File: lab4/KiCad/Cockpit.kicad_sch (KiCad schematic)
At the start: 24 parts, among them J30 CAN A isolation, J31 CAN A test, J34 CAN B isolation, J35 CAN B test, U30 MCP2515T-I/ST, U31 SN65HVD231MDREP, U34 MCP2515T-I/ST, U35 SN65HVD231MDREP, Y30 16 MHz, Y34 16 MHz

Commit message: Integrate Lab 4 MCU support, diagnostics and hierarchical connections
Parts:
- added C700: 22u /16V, Capacitor_SMD:C_0805_2012Metric, symbol Device:C
- added C701: 100n, Capacitor_SMD:C_0603_1608Metric, symbol Device:C
- added C702: 100n TEST, Capacitor_SMD:C_0603_1608Metric, symbol Device:C
- added D710: STATUS green, LED_SMD:LED_0603_1608Metric, symbol Device:LED
- added D711: ERR red, LED_SMD:LED_0603_1608Metric, symbol Device:LED
- added D712: DEG_A yellow, LED_SMD:LED_0603_1608Metric, symbol Device:LED
- added D713: DEG_B yellow, LED_SMD:LED_0603_1608Metric, symbol Device:LED
- added J70: Raspberry Pi4 GPIO, Connector_PinSocket_2.54mm:PinSocket_2x20_P2.54mm_Vertical, symbol Lab4_Logic:Pi4_Powered_Header
- added J703: LAB3 rows 1-13, Connector_PinHeader_2.54mm:PinHeader_1x13_P2.54mm_Vertical, symbol Connector_Generic:Conn_01x13
- added J704: Pi extra probes, Connector_PinHeader_2.54mm:PinHeader_1x05_P2.54mm_Vertical, symbol Connector_Generic:Conn_01x05
- added R700: 10k TEST pullup, Resistor_SMD:R_0603_1608Metric, symbol Device:R
- added R710, R711, R712, R713: 1k, Resistor_SMD:R_0603_1608Metric, symbol Device:R
- added SW70: SWT0210-045026GSA, symbol Switch:SW_Push
- U30, U34: symbol Interface_CAN_LIN:MCP2515-xST -> Lab4_Logic:MCP2515_TSSOP20
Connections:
- net +3V3: now also R700.1
- net GND: now also C700.2, C701.2, C702.2, D710.1 (K), D711.1 (K), D712.1 (K), D713.1 (K), J70.14 (GND), J70.20 (GND), J70.25 (GND), J70.30 (GND), J70.34 (GND), J70.39 (GND), J70.6 (GND), J70.9 (GND), J703.1 (Pin_1), J703.2 (Pin_2), J704.1 (Pin_1), J704.2 (Pin_2), SW70.2
- net PI_CS_A: now also J70.24 (~{CE0}_SPI0/GPIO08)
- net PI_CS_B: now also J70.26 (~{CE1}_SPI0/GPIO07)
- net PI_INT_A: now also J70.22 (GPIO25/SDIO_DAT1)
- net PI_INT_B: now also J70.18 (GPIO24/SDIO_DAT0)
- net PI_MISO: now also J70.21 (MISO_SPI0/GPIO09)
- net PI_MOSI: now also J70.19 (MOSI_SPI0/GPIO10)
- net PI_SCK: now also J70.23 (SCLK_SPI0/GPIO11)
- new net: J70.1 (3V3), J70.17 (3V3)
- new net +5V: C700.1, C701.1, J70.2 (5V), J70.4 (5V)
- new net PI_CMD_TX_MARKER: J70.13 (GPIO27/SDIO_DAT3), J703.4 (Pin_4)
- new net PI_DEG_A_LED: J70.29 (GPCLK1/GPIO05), J703.7 (Pin_7), R712.1
- new net PI_DEG_A_LED_ANODE: D712.2 (A), R712.2
- new net PI_DEG_B_LED: J70.31 (GPCLK2/GPIO06), J703.8 (Pin_8), R713.1
- new net PI_DEG_B_LED_ANODE: D713.2 (A), R713.2
- new net PI_ERROR_LED: J70.32 (GPIO12/PWM0), J704.4 (Pin_4), R711.1
- new net PI_ERROR_LED_ANODE: D711.2 (A), R711.2
- new net PI_SELFTEST_BUTTON: C702.1, J70.36 (GPIO16/SPI1_~{CE2}), J704.3 (Pin_3), R700.2, SW70.1
- new net PI_STATUS_LED: J70.33 (GPIO13/PWM1), J704.5 (Pin_5), R710.1
- new net PI_STATUS_LED_ANODE: D710.2 (A), R710.2
- new net PI_TX_A_MARKER: J70.15 (GPIO22/SDIO_CLK), J703.5 (Pin_5)
- new net PI_TX_B_MARKER: J70.16 (GPIO23/SDIO_CMD), J703.6 (Pin_6)
- new net PI_UDP_RX_MARKER: J70.11 (GPIO17/SPI1_~{CE1}), J703.3 (Pin_3)
- no-connect marks 12 -> 31
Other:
- note added: "All Pi GPIOs are 3.3V signals. Header pin number is NOT BCM GPIO number. Independent board 3.3V supplies the six CAN interfaces. A=CE0/IRQ25; B=CE1/IRQ24; confirm Linux labels against the installed overlay."
- note added: "Local bypass is not a load-step proof. Pi bulk capacitance / rail transient test remains open."
- note added: "Pins 2/4 receive board 5.1V. Pi 3.3V pins 1/17 are NOT joined to board 3.3V. Do not attach independent USB-C power while board 5.1V is connected. Confirm socket orientation with a 1:1 print and the actual Pi before routing."
- note added: "RASPBERRY PI 4 - 40-pin board socket"
- note added: "Rows 9-13 intentionally unused on Pi (Lab3 p17). Two GND pins per probe group. Active-high LED outputs. Physical reachability is a layout check, not established by this schematic."
- note added: "Shared rails and CAN backbone connect through the root sheet. SPI, clocks and reset stay within each zone."
- note removed: "HOST INTERFACE (to be integrated with the bare MCU / Pi header) SPI0: BCM11=SCK, BCM9=MISO, BCM10=MOSI; BCM8=CE0, BCM7=CE1. INT pins: verify against Pi configuration. These named nets are LOCAL to this zone. All +3V3 / +5V / GND / CAN backbone nets need hierarchy ports before full-board integration."
- title: Cockpit zone - dual CAN -> Cockpit zone - integrated logic and interfaces

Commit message: Update Lab 4 circuits, assembly BOMs and measured PCB placement
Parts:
- C300, C301, C340, C341: value Cload TBD -> 18p C0G 50V; Design status (none) -> CL=12pF; equal 18pF caps assume 3pF effective stray; tune a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; MPN (none) -> GRM1885C1H180JA01D
- J70: footprint Connector_PinSocket_2.54mm:PinSocket_2x20_P2.54mm_Vertical -> Lab4_Mechanical:Samtec_ESQ-120-44_2x20_P2.54mm_H18.67; Design status Physical header numbering; select mating height/orientation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 -> Bottom-mounted direct Pi socket; 22mm nominal board gap; ve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; MPN TBD 2x20 female socket -> ESQ-120-44-L-D
- U31, U35: value SN65HVD231MDREP -> SN65HVD231DR; Design status Course Oct 16 substitution; verify exact supplied ordering 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 -> TI verified SOIC-8 order code; confirm course-stock equival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; MPN SN65HVD231MDREP -> SN65HVD231DR

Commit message: Prepare Lab 4 review package and align course assembly plan
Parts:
- C302, C303, C304, C342, C343, C344: Design status (none) -> Preliminary; verify before fabrication; MPN (none) -> KGM15AR71C104KT
- J31, J35, U30, U34: Design status (none) -> Preliminary; verify before fabrication
- R300, R301, R340, R341: Design status (none) -> Preliminary; verify before fabrication; MPN (none) -> CRCW060310K0FKEA
- SW70: Design status Electrical circuit placed; exact GCT footprint drawing stil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 -> GCT drawing located (25-Apr-2025); contact-pair/pad geometr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
- U31, U35: Design status TI verified SOIC-8 order code; confirm course-stock equival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 -> Exact MPN appears in course v3 stock list; TI SOIC-8 pinout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

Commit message: Add verified GCT switch footprints and refresh Lab 4 checks
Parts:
- SW70: footprint (none) -> Lab4_Switches:GCT_SWT0210_4.5x4.5mm; Design status GCT drawing located (25-Apr-2025); contact-pair/pad geometr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 -> GCT A1 drawing verified: physical terminals 1/2 -> logical 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

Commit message: Complete MCU routing and refine feedback and power transitions
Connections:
- net at J70.1 (3V3): no longer J70.17 (3V3)
- no-connect marks 31 -> 32

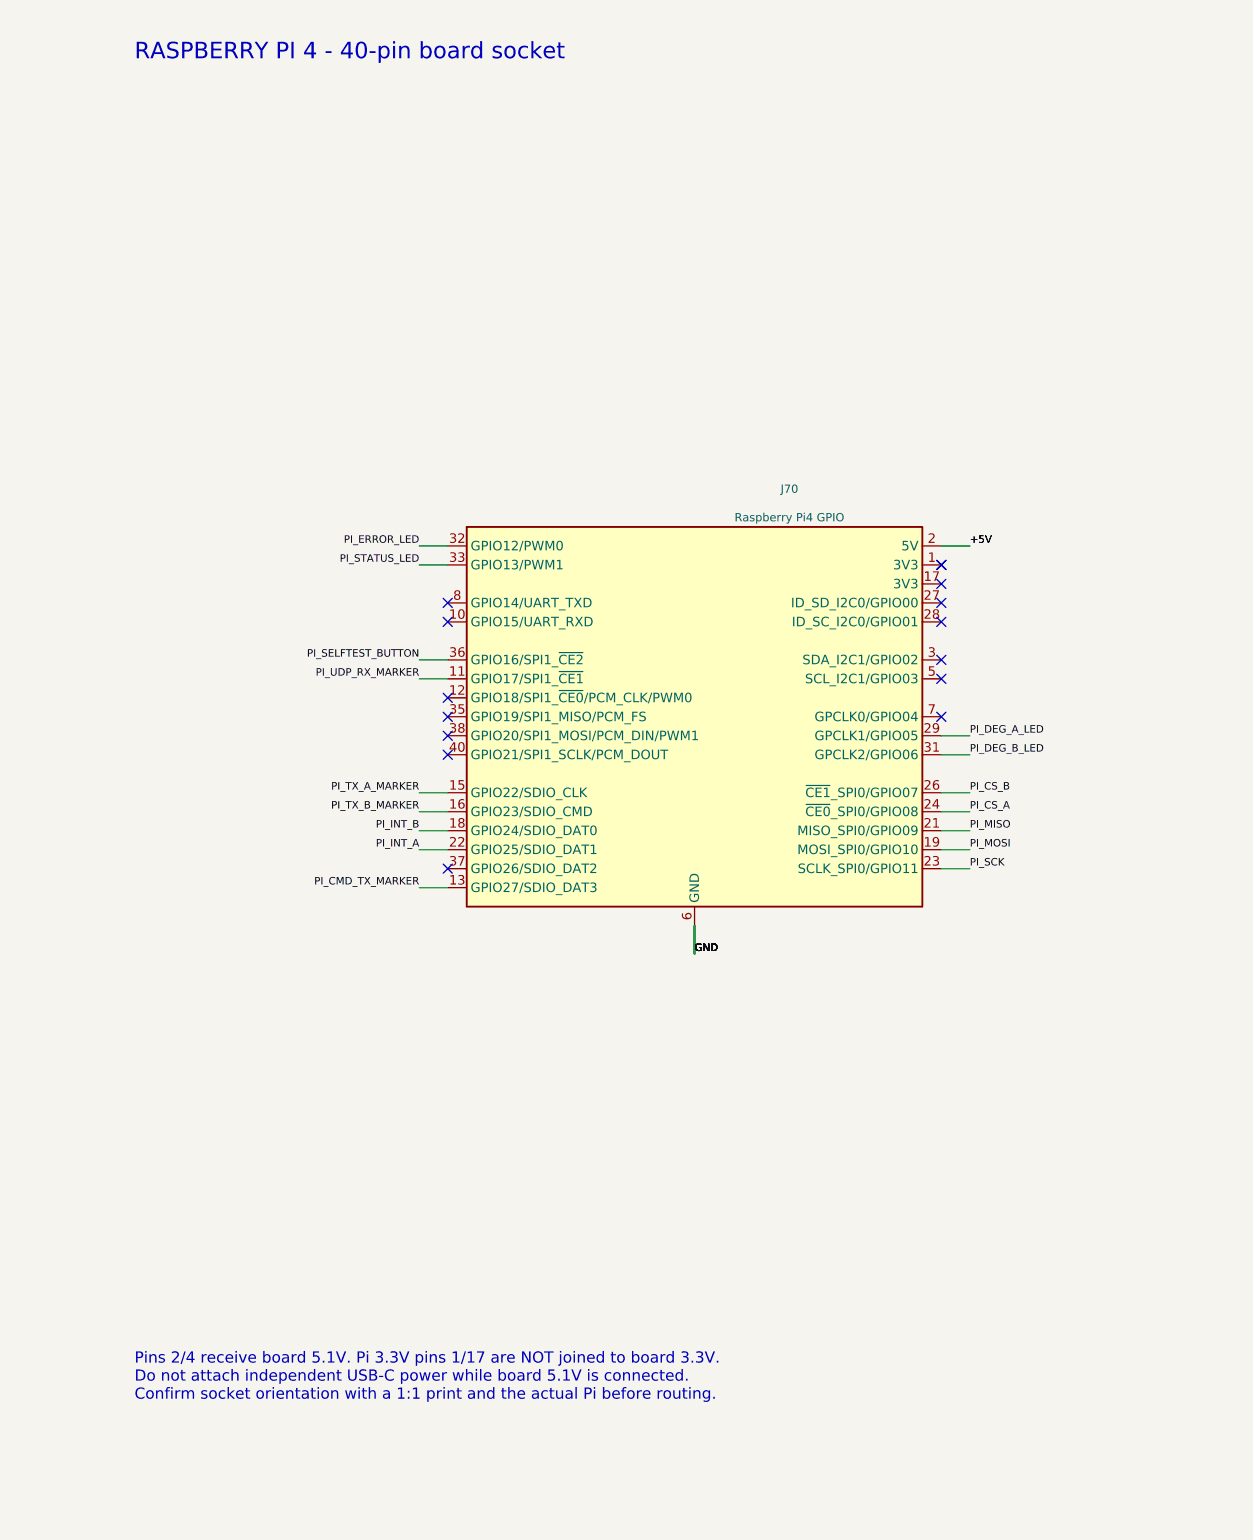
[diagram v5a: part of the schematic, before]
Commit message: Apply hole-edge clearance and integrate heatsink and encoder supply
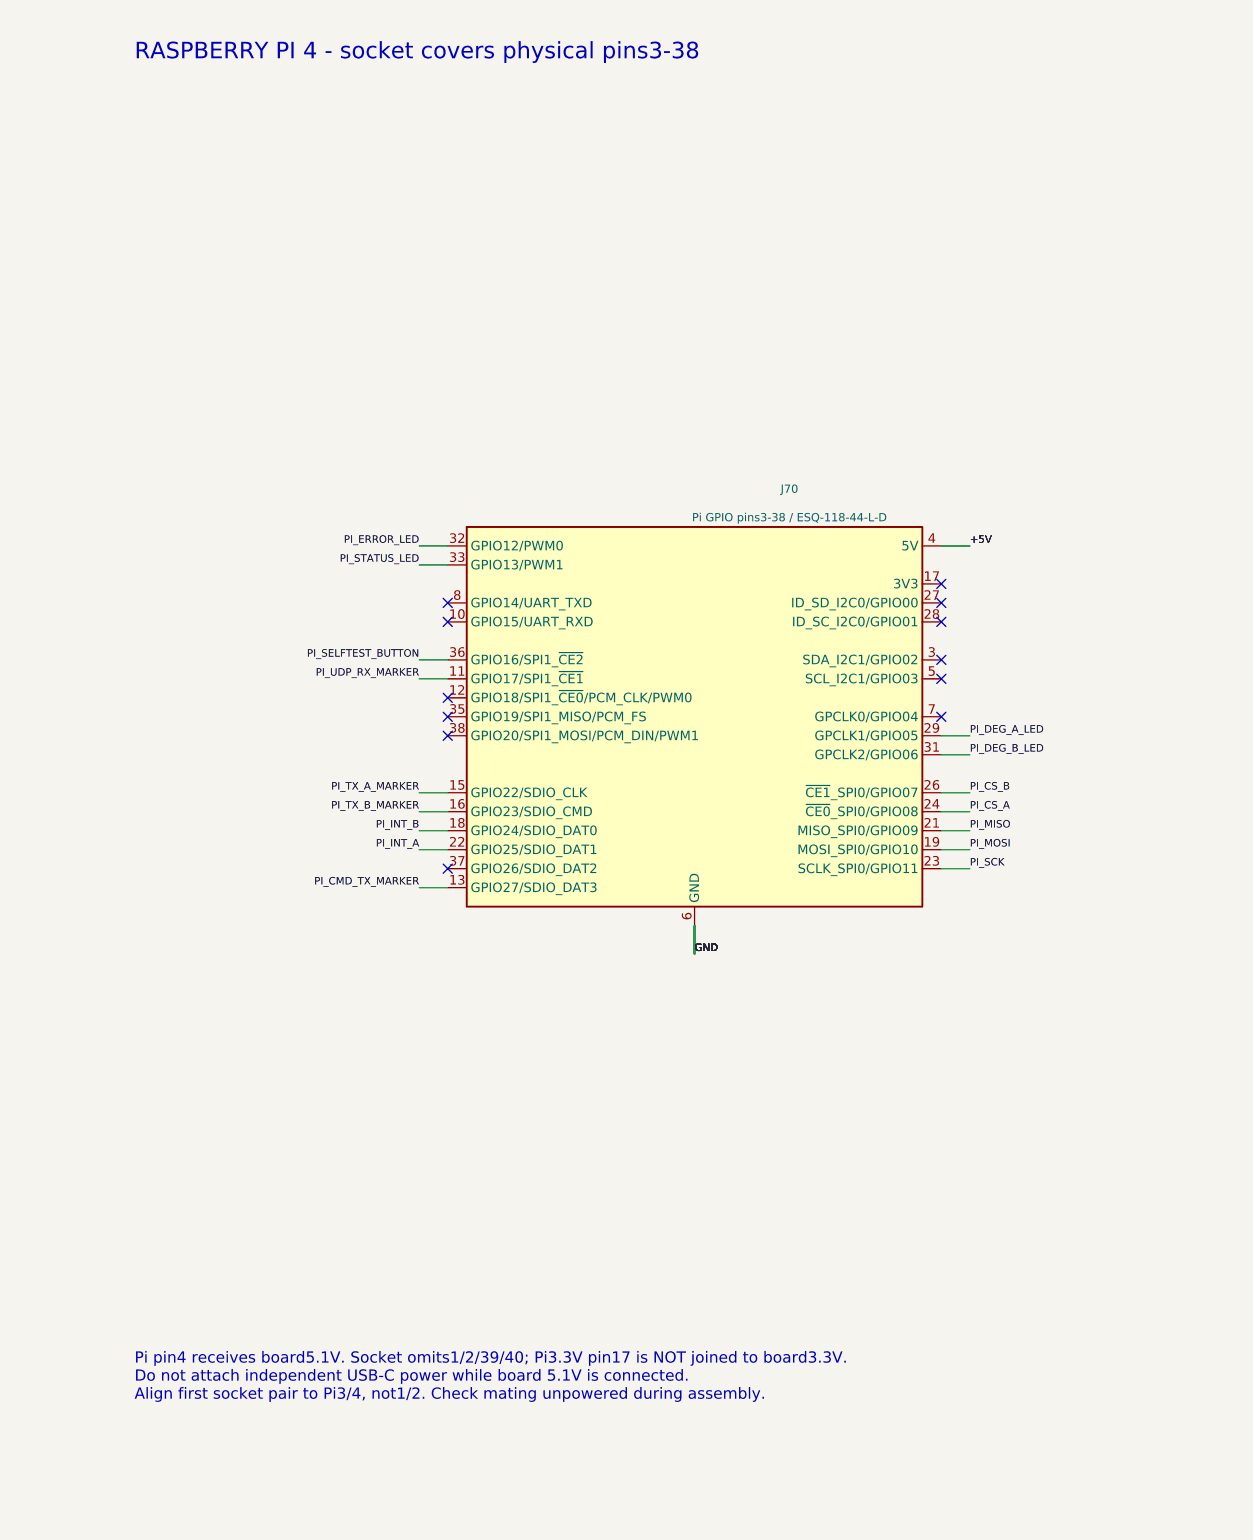
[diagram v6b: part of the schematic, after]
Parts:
- J70: value Raspberry Pi4 GPIO -> Pi GPIO pins3-38 / ESQ-118-44-L-D; footprint Lab4_Mechanical:Samtec_ESQ-120-44_2x20_P2.54mm_H18.67 -> Lab4_Mechanical:Samtec_ESQ-118-44_2x18_PiPins3-38_H18.67; symbol Lab4_Logic:Pi4_Powered_Header -> Lab4_Logic:Pi4_Powered_Header_3_to_38; Design status Bottom-mounted direct Pi socket; 22mm nominal board gap; ve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 -> 36-contact bottom socket on Pi pins3-38; first/last Pi pin 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; MPN ESQ-120-44-L-D -> ESQ-118-44-L-D
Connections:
- net +5V: no longer J70.2 (5V)
- net GND: no longer J70.39 (GND)
- no-connect marks 32 -> 29
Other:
- note added: "Pi pin4 receives board5.1V. Socket omits1/2/39/40; Pi3.3V pin17 is NOT joined to board3.3V. Do not attach independent USB-C power while board 5.1V is connected. Align first socket pair to Pi3/4, not1/2. Check mating unpowered during assembly."
- note added: "RASPBERRY PI 4 - socket covers physical pins3-38"
- note removed: "Pins 2/4 receive board 5.1V. Pi 3.3V pins 1/17 are NOT joined to board 3.3V. Do not attach independent USB-C power while board 5.1V is connected. Confirm socket orientation with a 1:1 print and the actual Pi before routing."
- note removed: "RASPBERRY PI 4 - 40-pin board socket"
